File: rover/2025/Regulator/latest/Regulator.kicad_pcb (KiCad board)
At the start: 4 copper layers, 46.4 x 32.6 mm, 31 parts, among them J1 ETH-RJHSE508102, J2 Conn_01x01_Pin, J3 Conn_01x01_Pin, J4 Conn_01x01_Pin, J5 Conn_01x01_Pin, J6 ETH-RJHSE5081, U1 DC_DC-AP64501

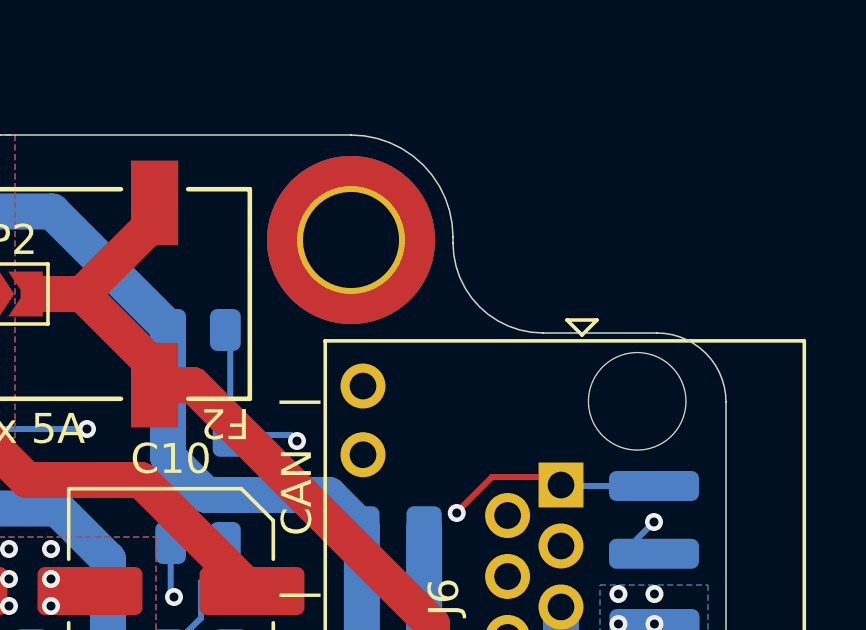
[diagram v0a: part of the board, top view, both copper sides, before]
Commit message: Last touch before order for ARMJL, Regulator and DDB + start of J345
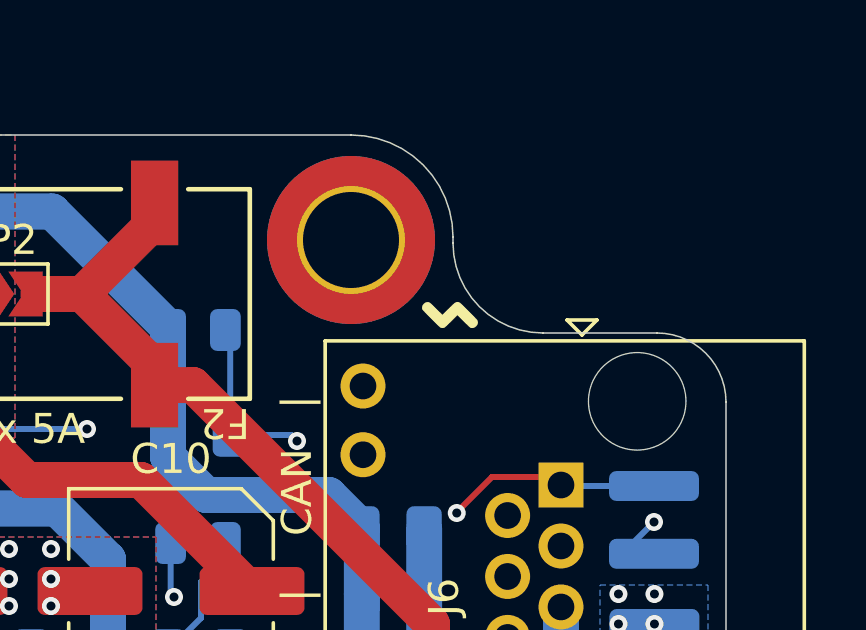
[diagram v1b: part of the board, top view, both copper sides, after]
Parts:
- added G***: LOGO, LOGO, F.Cu at (62.6, 28.3)
- added G***: LOGO, LOGO, B.Cu at (35.3, 44.4)
- R4, R5: value 5.1k -> 1k
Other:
- board text added: "${CURRENT_DATE} ${GROUP_NAME} ${TEAM}"
- board text added: "${PROJECTNAME} REV${REVISION} by: ${AUTHOR}"

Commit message: Regulator Ready to order
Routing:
- added copper zone on In1.Cu, net GND
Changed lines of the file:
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@@
+		(net 1)
+		(net_name "GND")
+		(layers "F.Cu" "In1.Cu" "In2.Cu" "B.Cu")
+		(hatch edge 0.5)
+		(connect_pads
+			(clearance 0.5)
+		)
+		(min_thickness 0.25)
+		(filled_areas_thickness no)
+		(fill yes
+			(thermal_gap 0.5)
+			(thermal_bridge_width 2)
+		)
+		(polygon
+			(pts
+				(xy 25.5 21) (xy 72 20.9) (xy 72 53.5) (xy 25.6 53.6)
+			)
+		)
+	)
+	(zone
 		(net 1)
 		(net_name "GND")
@@
 			)
 		)
-	)
-	(zone
-		(net 1)
-		(net_name "GND")
-		(layer "In2.Cu")
-		(hatch edge 0.5)
-		(connect_pads
-			(clearance 0.5)
-		)
-		(min_thickness 0.25)
-		(filled_areas_thickness no)
-		(fill yes
-			(thermal_gap 0.5)
-			(thermal_bridge_width 2)
-		)
-		(polygon
-			(pts
-				(xy 25.5 21) (xy 71.4 21) (xy 71.4 53.6) (xy 25.6 53.6)
-			)
-		)

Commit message: PCBs ordered
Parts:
- removed C2: 22uF, Capacitor_SMD:C_0805_2012Metric_Pad1.18x1.45mm_HandSolder
- C1, C5, C6, C7: footprint Capacitor_SMD:C_0805_2012Metric_Pad1.18x1.45mm_HandSolder -> Capacitor_SMD:C_1210_3225Metric_Pad1.33x2.70mm_HandSolder
- C11: value 100uF (Opt) -> 100uF
- C9: value (Opt) -> (TBD)
- L1, R1, R3: value ~ -> (TBD)
- R4, R5: value 1k -> 5.1k
- R6: value 22.1k -> 5.1k; footprint Resistor_SMD:R_0805_2012Metric -> Resistor_SMD:R_0805_2012Metric_Pad1.20x1.40mm_HandSolder
- moved C5 1.25 mm to (60.9, 38.6)
- moved C7 0.75 mm to (60.9, 36.0)
- moved R2 0.75 mm to (41.4, 38.5)
- moved C1 0.64 mm to (54.0, 50.1)
- moved C6 0.30 mm to (41.4, 42.4)
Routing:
- net /CANH: track 58.0 -> 59.4 mm
- net Net-(JP2-A): track 51.5 -> 50.3 mm
- net Net-(JP1-B): track 33.8 -> 34.3 mm
